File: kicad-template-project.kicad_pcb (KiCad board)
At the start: 6 copper layers, 50 x 50 mm, 108 parts, among them J1 Conn_ST_STDC14, J2 Conn_01x12, J3 Conn_01x13, Q1 LMG2100R026, Q2 LMG2100R026, Q3 LMG2100R026, U1 MCS1823, U10 ADCS7476, U11 ADCS7476, U12 TPS54360DDA, U13 MIC5219YM5, U14 MIC5219YM5, U15 W25Q16JVSS, U2 MCS1823, U3 MCS1823, U4 ICE40UP5K-SG48ITR, U5 STM32L432KBUx, U6 ISO1044BD, U7 MIC5219YM5, U8 MLX90395xLW, U9 ADCS7476

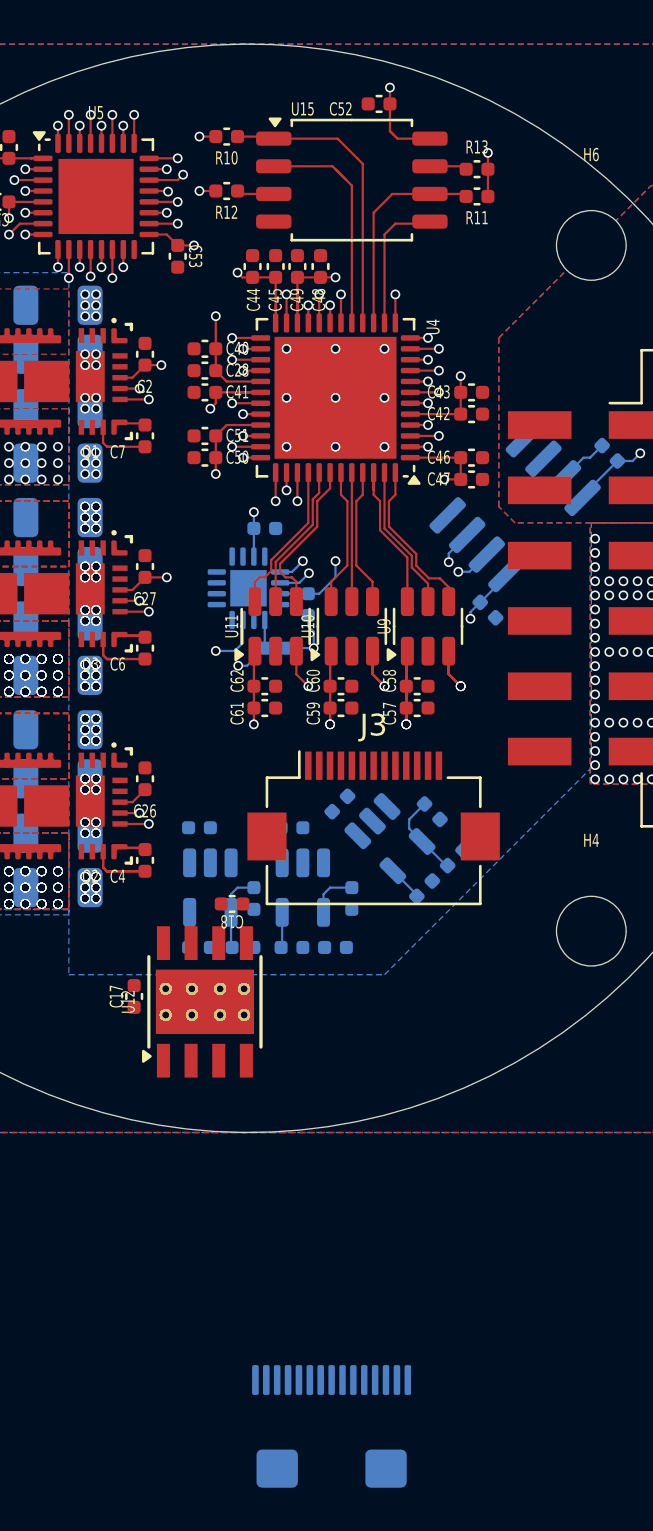
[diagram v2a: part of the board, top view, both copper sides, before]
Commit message: fix: finalized position of fpc programmer
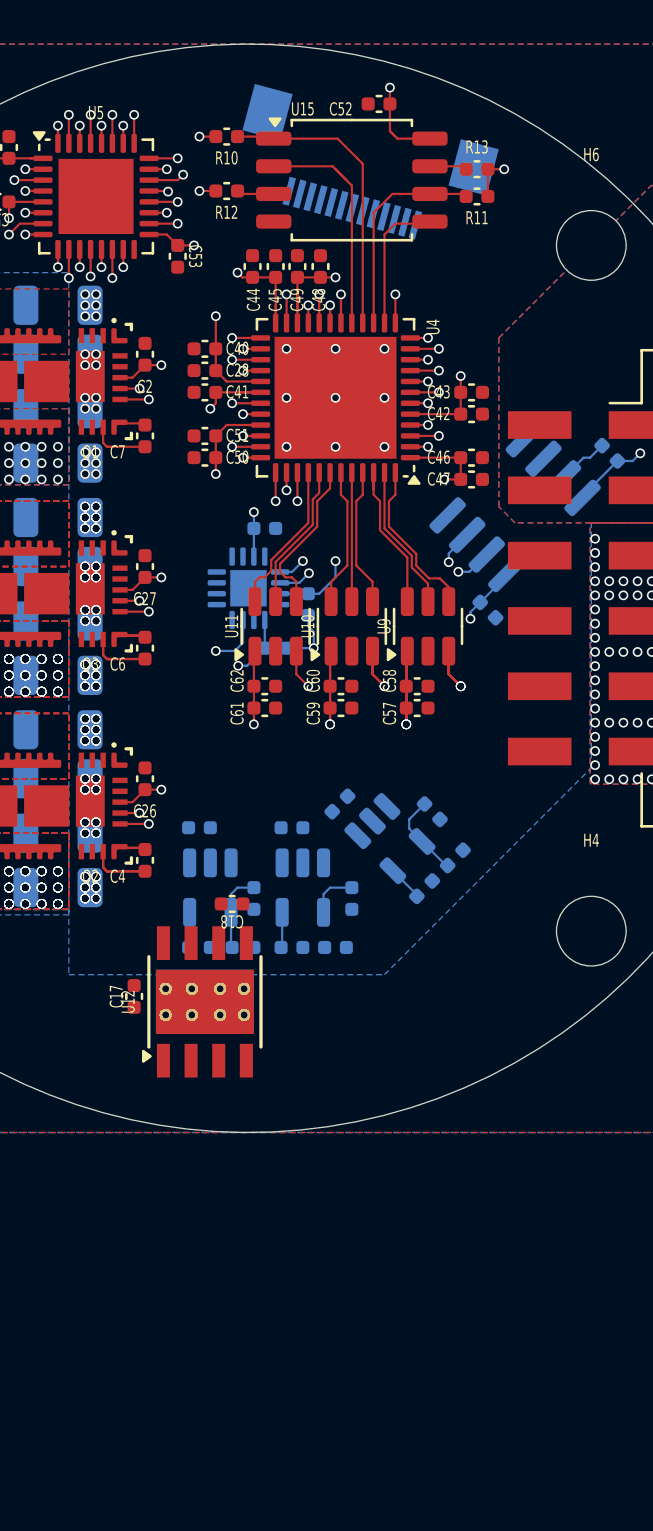
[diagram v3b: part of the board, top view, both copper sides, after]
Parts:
- removed J1: Conn_ST_STDC14, Connector_FFC-FPC:Molex_502231-1500_1x15-1SH_P0.5mm_Vertical
- J3: moved to B.Cu
- moved J3 29.3 mm to (135.2, 115.8), turned to -15 degrees
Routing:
- net VDD_5V: track 7.87 -> 8.37 mm, vias 2 -> 3
